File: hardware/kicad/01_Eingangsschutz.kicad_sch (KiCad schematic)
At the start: 0 parts

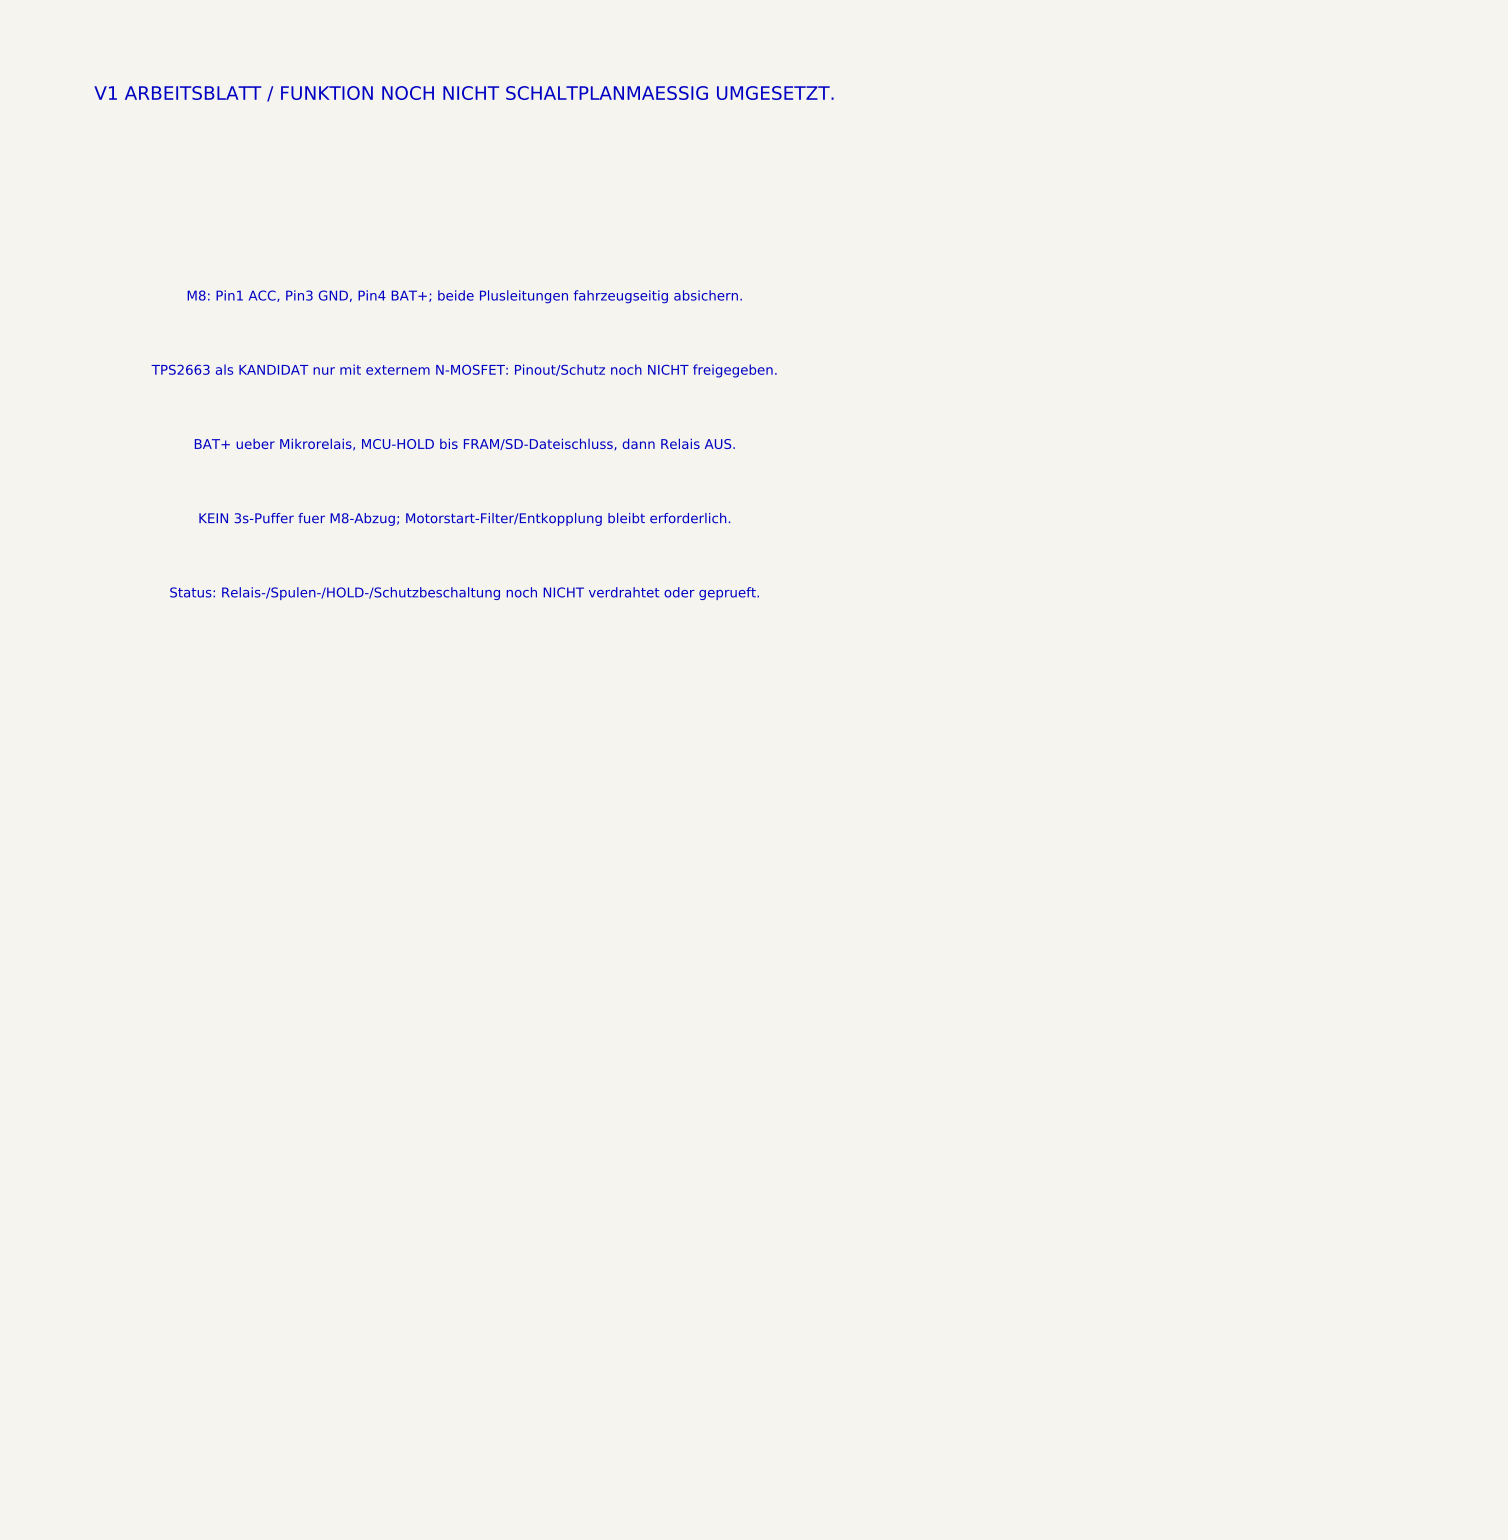
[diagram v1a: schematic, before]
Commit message: hardware(kicad): add Omron relay library footprint and staged coil driver on sheet 01
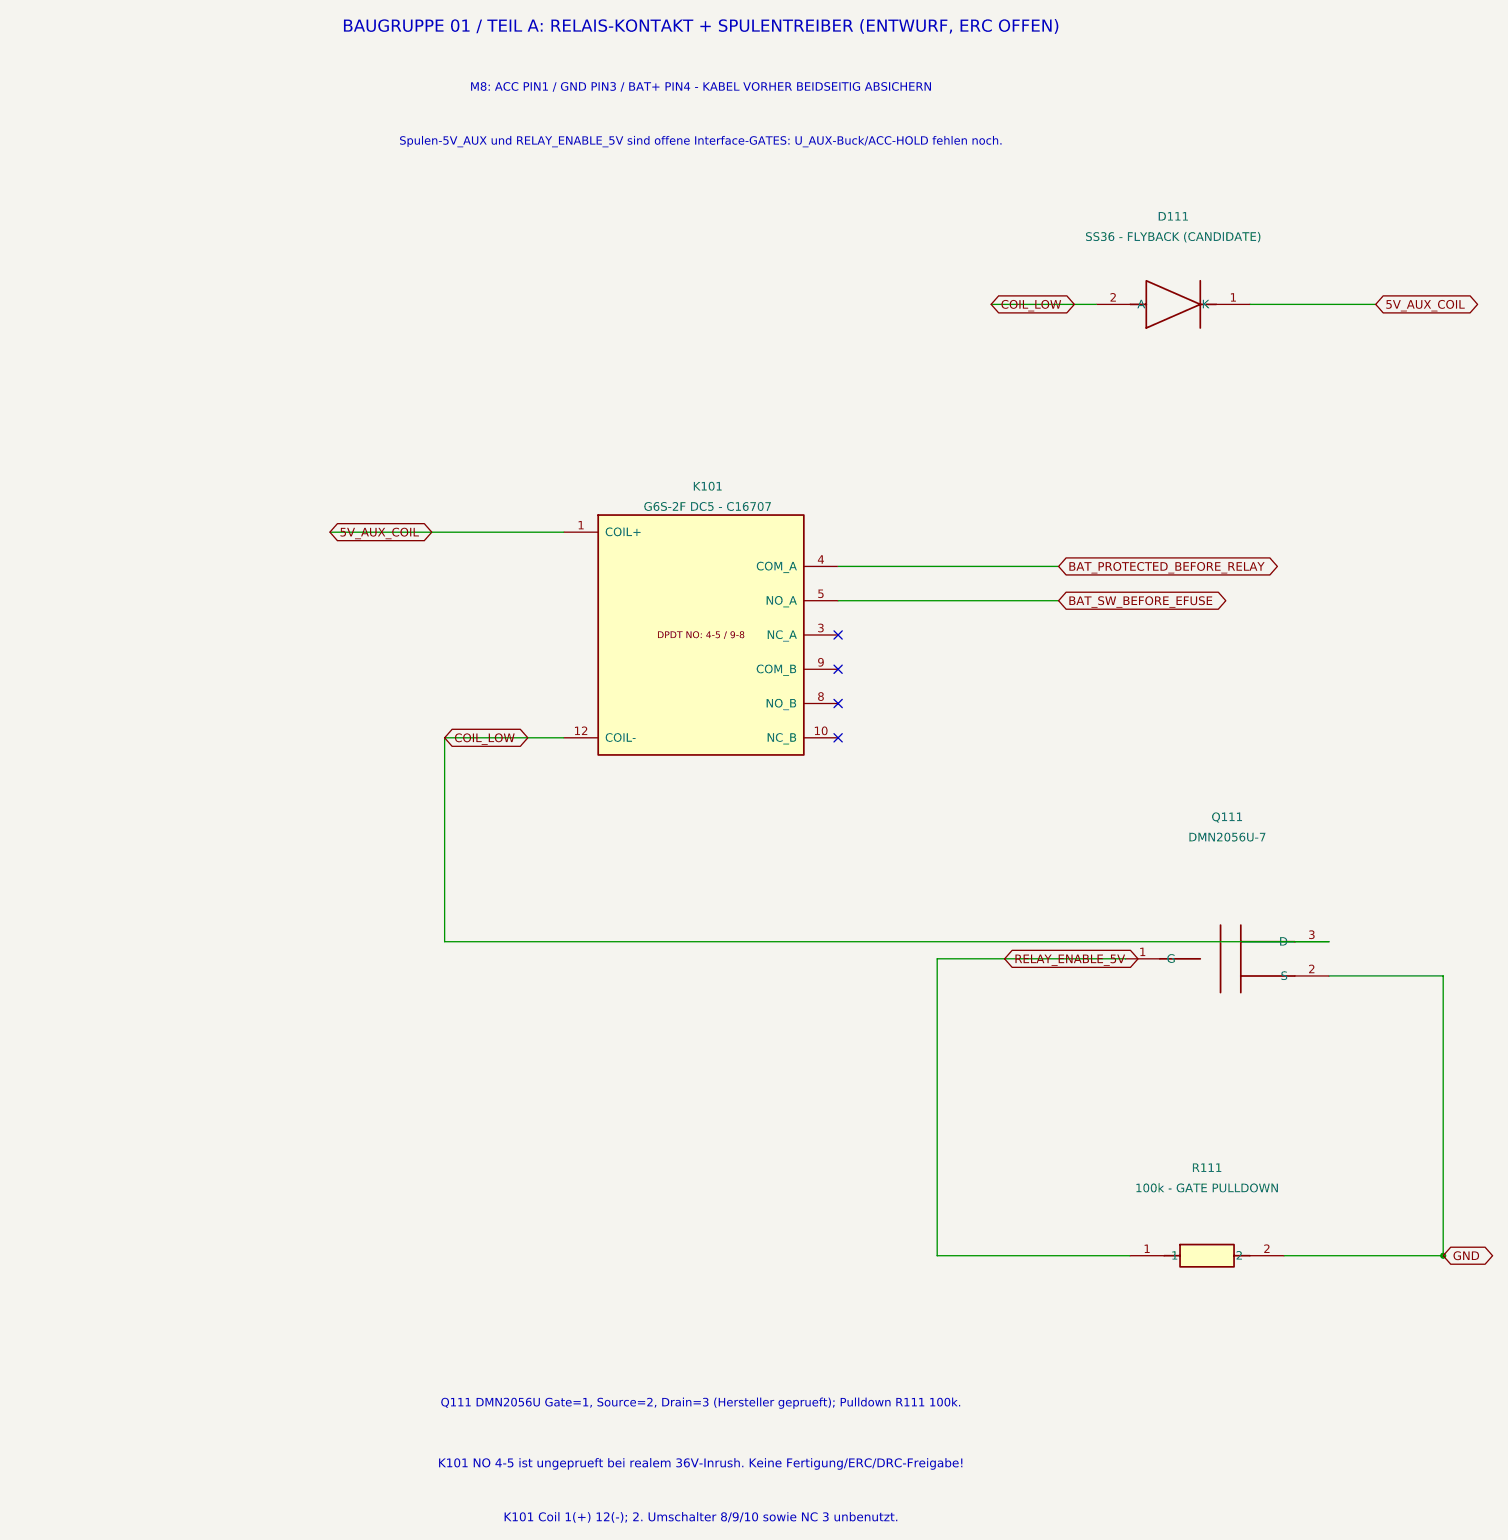
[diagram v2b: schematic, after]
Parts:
- added D111: SS36 - FLYBACK (CANDIDATE), Tripmaster:D_SMA_SS36, symbol Tripmaster_Sym:SCHOTTKY
- added K101: G6S-2F DC5 - C16707, Tripmaster:RLY101_Omron_G6S_2F, symbol TripTracer_V1:G6S_2F_DC5
- added Q111: DMN2056U-7, Tripmaster:Q1_Diodes_DMN2056U_7, symbol Tripmaster_Sym:NMOS
- added R111: 100k - GATE PULLDOWN, Tripmaster:R_1206_3216, symbol Tripmaster_Sym:R
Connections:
- new net 5V_AUX_COIL: D111.1 (K), K101.1 (COIL+)
- new net BAT_PROTECTED_BEFORE_RELAY: K101.4 (COM_A)
- new net BAT_SW_BEFORE_EFUSE: K101.5 (NO_A)
- new net COIL_LOW: D111.2 (A), K101.12 (COIL-), Q111.3 (D)
- new net GND: Q111.2 (S), R111.2
- new net RELAY_ENABLE_5V: Q111.1 (G), R111.1
- no-connect marks 0 -> 4
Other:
- note added: "BAUGRUPPE 01 / TEIL A: RELAIS-KONTAKT + SPULENTREIBER (ENTWURF, ERC OFFEN)"
- note added: "K101 Coil 1(+) 12(-); 2. Umschalter 8/9/10 sowie NC 3 unbenutzt."
- note added: "K101 NO 4-5 ist ungeprueft bei realem 36V-Inrush. Keine Fertigung/ERC/DRC-Freigabe!"
- note added: "M8: ACC PIN1 / GND PIN3 / BAT+ PIN4 - KABEL VORHER BEIDSEITIG ABSICHERN"
- note added: "Q111 DMN2056U Gate=1, Source=2, Drain=3 (Hersteller geprueft); Pulldown R111 100k."
- note added: "Spulen-5V_AUX und RELAY_ENABLE_5V sind offene Interface-GATES: U_AUX-Buck/ACC-HOLD fehlen noch."
- note removed: "BAT+ ueber Mikrorelais, MCU-HOLD bis FRAM/SD-Dateischluss, dann Relais AUS."
- note removed: "KEIN 3s-Puffer fuer M8-Abzug; Motorstart-Filter/Entkopplung bleibt erforderlich."
- note removed: "M8: Pin1 ACC, Pin3 GND, Pin4 BAT+; beide Plusleitungen fahrzeugseitig absichern."
- note removed: "Status: Relais-/Spulen-/HOLD-/Schutzbeschaltung noch NICHT verdrahtet oder geprueft."
- note removed: "TPS2663 als KANDIDAT nur mit externem N-MOSFET: Pinout/Schutz noch NICHT freigegeben."
- note removed: "V1 ARBEITSBLATT / FUNKTION NOCH NICHT SCHALTPLANMAESSIG UMGESETZT."
- title: TripTracer V1 – ACC / BAT+ / Mikrorelais / eFuse -> TripTracer V1 - ACC/BAT+ Eingangsschutz und Relais
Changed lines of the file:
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@@
 (kicad_sch (version 20250114) (generator "eeschema")
- (paper "A3") (title_block (title "TripTracer V1 – ACC / BAT+ / Mikrorelais / eFuse") (date "2026-10-13") (rev "a0 / NOCH NICHT VERDRAHTET"))
- (text "V1 ARBEITSBLATT / FUNKTION NOCH NICHT SCHALTPLANMAESSIG UMGESETZT." (at 165 35 0) (effects (font (size 2 2))))
- (text "M8: Pin1 ACC, Pin3 GND, Pin4 BAT+; beide Plusleitungen fahrzeugseitig absichern." (at 165 65 0) (effects (font (size 1.45 1.45))))
-(text "TPS2663 als KANDIDAT nur mit externem N-MOSFET: Pinout/Schutz noch NICHT freigegeben." (at 165 76 0) (effects (font (size 1.45 1.45))))
-(text "BAT+ ueber Mikrorelais, MCU-HOLD bis FRAM/SD-Dateischluss, dann Relais AUS." (at 165 87 0) (effects (font (size 1.45 1.45))))
-(text "KEIN 3s-Puffer fuer M8-Abzug; Motorstart-Filter/Entkopplung bleibt erforderlich." (at 165 98 0) (effects (font (size 1.45 1.45))))
-(text "Status: Relais-/Spulen-/HOLD-/Schutzbeschaltung noch NICHT verdrahtet oder geprueft." (at 165 109 0) (effects (font (size 1.45 1.45))))
- (sheet_instances (path "/" (page "2"))) (embedded_fonts no)
+ (paper "A3")
+ (title_block (title "TripTracer V1 - ACC/BAT+ Eingangsschutz und Relais") (date "2026-10-13") (rev "a1 / RELAIS-TEILENTWURF - NICHT ERC-GEPRUEFT"))
+ (symbol (lib_id "TripTracer_V1:G6S_2F_DC5") (at 200 115 0) (unit 1) (exclude_from_sim no) (in_bom yes) (on_board yes) (dnp no)
+ (property "Reference" "K101" (at 201 93 0) (effects (font (size 1.27 1.27))))
+ (property "Value" "G6S-2F DC5 - C16707" (at 201 96 0) (effects (font (size 1.27 1.27))))
+ (property "Footprint" "Tripmaster:RLY101_Omron_G6S_2F" (at 200 115 0) (effects (font (size 1.27 1.27)) (hide yes)))
+ (pin "1") (pin "12") (pin "4") (pin "5") (pin "3") (pin "9") (pin "8") (pin "10")
+ (instances (project "TripTracer_V1" (path "/a26d9b0c-7f10-4e5a-a65f-000000000064/a26d9b0c-7f10-4e5a-a65f-000000000065" (reference "K101") (unit 1)))))
+(symbol (lib_id "Tripmaster_Sym:NMOS") (at 278 163 0) (unit 1) (exclude_from_sim no) (in_bom yes) (on_board yes) (dnp no)
+ (property "Reference" "Q111" (at 278 142 0) (effects (font (size 1.27 1.27))))
+ (property "Value" "DMN2056U-7" (at 278 145 0) (effects (font (size 1.27 1.27))))
+ (property "Footprint" "Tripmaster:Q1_Diodes_DMN2056U_7" (at 278 163 0) (effects (font (size 1.27 1.27)) (hide yes)))
+ (pin "1") (pin "2") (pin "3")
+ (instances (project "TripTracer_V1" (path "/a26d9b0c-7f10-4e5a-a65f-000000000064/a26d9b0c-7f10-4e5a-a65f-000000000065" (reference "Q111") (unit 1)))))
+(symbol (lib_id "Tripmaster_Sym:SCHOTTKY") (at 270 66 0) (unit 1) (exclude_from_sim no) (in_bom yes) (on_board yes) (dnp no)
+ (property "Reference" "D111" (at 270 53 0) (effects (font (size 1.27 1.27))))
+ (property "Value" "SS36 - FLYBACK (CANDIDATE)" (at 270 56 0) (effects (font (size 1.27 1.27))))
+ (property "Footprint" "Tripmaster:D_SMA_SS36" (at 270 66 0) (effects (font (size 1.27 1.27)) (hide yes)))
+ (pin "1") (pin "2")
+ (instances (project "TripTracer_V1" (path "/a26d9b0c-7f10-4e5a-a65f-000000000064/a26d9b0c-7f10-4e5a-a65f-000000000065" (reference "D111") (unit 1)))))
+(symbol (lib_id "Tripmaster_Sym:R") (at 275 207 0) (unit 1) (exclude_from_sim no) (in_bom yes) (on_board yes) (dnp no)
+ (property "Reference" "R111" (at 275 194 0) (effects (font (size 1.27 1.27))))
+ (property "Value" "100k - GATE PULLDOWN" (at 275 197 0) (effects (font (size 1.27 1.27))))
+ (property "Footprint" "Tripmaster:R_1206_3216" (at 275 207 0) (effects (font (size 1.27 1.27)) (hide yes)))
+ (pin "1") (pin "2")
+ (instances (project "TripTracer_V1" (path "/a26d9b0c-7f10-4e5a-a65f-000000000064/a26d9b0c-7f10-4e5a-a65f-000000000065" (reference "R111") (unit 1)))))
+ (wire (pts (xy 145 99.76) (xy 179.68 99.76)) (stroke (width 0) (type default)))
+(global_label "5V_AUX_COIL" (shape bidirectional) (at 145 99.76 0) (effects (font (size 1.27 1.27)) (justify left)))
+(wire (pts (xy 179.68 130.24) (xy 162 130.24)) (stroke (width 0) (type default)))
+(wire (pts (xy 162 130.24) (xy 162 160.46)) (stroke (width 0) (type default)))
+(wire (pts (xy 162 160.46) (xy 293.08 160.46)) (stroke (width 0) (type default)))
+(global_label "COIL_LOW" (shape bidirectional) (at 162 130.24 0) (effects (font (size 1.27 1.27)) (justify left)))
+(wire (pts (xy 220.32 104.84) (xy 253 104.84)) (stroke (width 0) (type default)))
+(global_label "BAT_PROTECTED_BEFORE_RELAY" (shape bidirectional) (at 253 104.84 0) (effects (font (size 1.27 1.27)) (justify left)))
+(wire (pts (xy 220.32 109.92) (xy 253 109.92)) (stroke (width 0) (type default)))
+(global_label "BAT_SW_BEFORE_EFUSE" (shape bidirectional) (at 253 109.92 0) (effects (font (size 1.27 1.27)) (justify left)))
+(no_connect (at 220.32 115))
+(no_connect (at 220.32 120.08))
+(no_connect (at 220.32 125.16))
+(no_connect (at 220.32 130.24))
+(wire (pts (xy 293.08 165.54) (xy 310 165.54)) (stroke (width 0) (type default)))
+(wire (pts (xy 310 165.54) (xy 310 207)) (stroke (width 0) (type default)))
+(global_label "GND" (shape bidirectional) (at 310 207 0) (effects (font (size 1.27 1.27)) (justify left)))
+(wire (pts (xy 262.92 163) (xy 245 163)) (stroke (width 0) (type default)))
+(global_label "RELAY_ENABLE_5V" (shape bidirectional) (at 245 163 0) (effects (font (size 1.27 1.27)) (justify left)))
+(wire (pts (xy 245 163) (xy 235 163)) (stroke (width 0) (type default)))
+(wire (pts (xy 235 163) (xy 235 207)) (stroke (width 0) (type default)))
+(wire (pts (xy 235 207) (xy 263.57 207)) (stroke (width 0) (type default)))
+(wire (pts (xy 286.43 207) (xy 310 207)) (stroke (width 0) (type default)))
+(junction (at 310 207) (diameter 0) (color 0 0 0 0))
+(wire (pts (xy 243 66) (xy 258.57 66)) (stroke (width 0) (type default)))
+(global_label "COIL_LOW" (shape bidirectional) (at 243 66 0) (effects (font (size 1.27 1.27)) (justify left)))
+(wire (pts (xy 281.43 66) (xy 300 66)) (stroke (width 0) (type default)))
+(global_label "5V_AUX_COIL" (shape bidirectional) (at 300 66 0) (effects (font (size 1.27 1.27)) (justify left)))
+(text "BAUGRUPPE 01 / TEIL A: RELAIS-KONTAKT + SPULENTREIBER (ENTWURF, ERC OFFEN)" (at 200 25 0) (effects (font (size 1.8 1.8))))
+(text "M8: ACC PIN1 / GND PIN3 / BAT+ PIN4 - KABEL VORHER BEIDSEITIG ABSICHERN" (at 200 34 0) (effects (font (size 1.25 1.25))))
+(text "Spulen-5V_AUX und RELAY_ENABLE_5V sind offene Interface-GATES: U_AUX-Buck/ACC-HOLD fehlen noch." (at 200 42 0) (effects (font (size 1.23 1.23))))
+(text "Q111 DMN2056U Gate=1, Source=2, Drain=3 (Hersteller geprueft); Pulldown R111 100k." (at 200 229 0) (effects (font (size 1.25 1.25))))
+(text "K101 NO 4-5 ist ungeprueft bei realem 36V-Inrush. Keine Fertigung/ERC/DRC-Freigabe!" (at 200 238 0) (effects (font (size 1.3 1.3))))
+(text "K101 Coil 1(+) 12(-); 2. Umschalter 8/9/10 sowie NC 3 unbenutzt." (at 200 246 0) (effects (font (size 1.3 1.3))))
+ (sheet_instances (path "/" (page "2")))
+ (embedded_fonts no)
 )
